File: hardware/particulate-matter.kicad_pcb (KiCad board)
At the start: 2 copper layers, 70 x 40 mm, 36 parts, among them P1 CON-SENSOR2, P2 BOOT, P3 DEBUG, U1 XMC1XXX48, U2 DRILL, U3 DRILL, U4 DRILL, U5 DRILL, U6 PMS7003, X1 16MHz

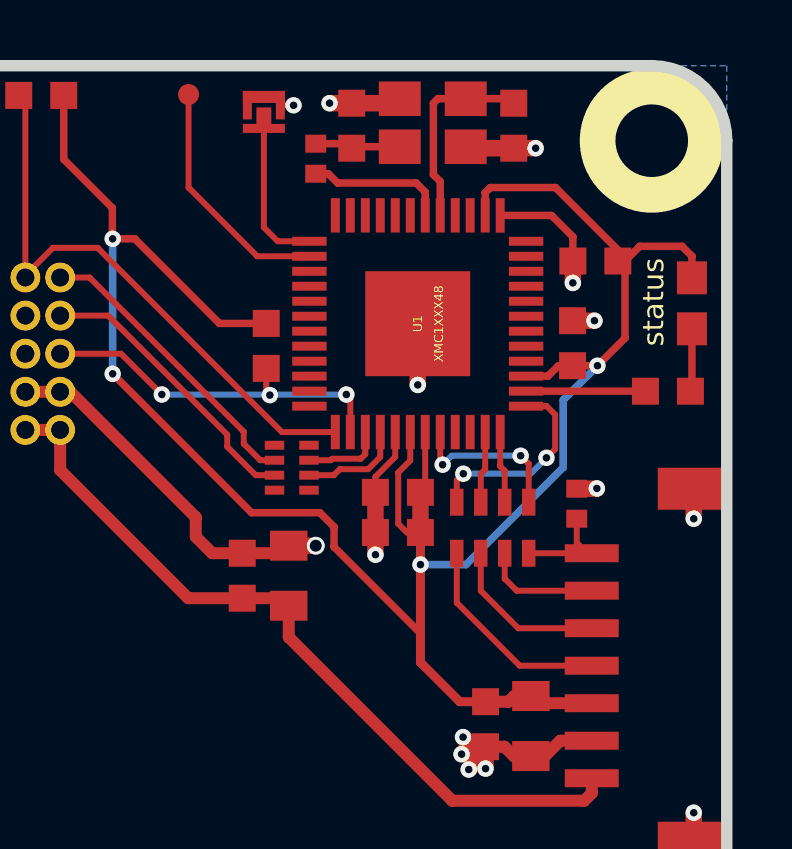
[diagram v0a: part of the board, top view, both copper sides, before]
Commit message: Remove R2, change footprint of RP1
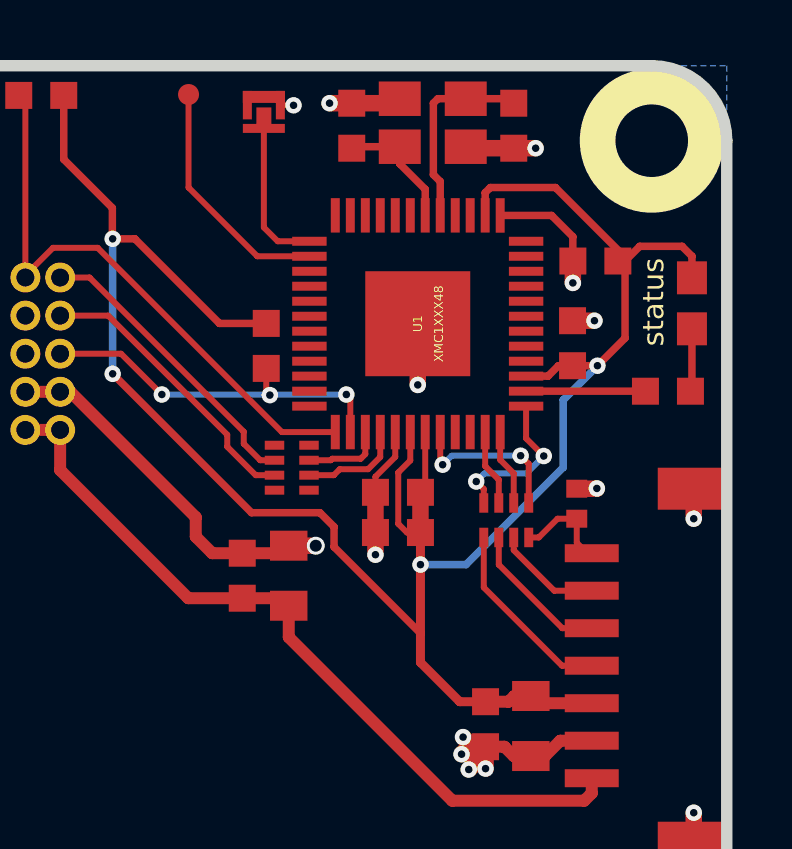
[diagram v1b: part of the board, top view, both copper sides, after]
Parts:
- removed R9: 0, kicad-libraries:R0402F
- RP1: footprint kicad-libraries:0603X4 -> kicad-libraries:4X0402
- moved RP1 0.51 mm to (163.4, 80.2), turned to 0 degrees
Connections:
- U1 pad 42: Net-(R9-Pad1) -> Net-(C9-Pad1)
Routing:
- net Net-(R9-Pad1): track 4.68 -> 0.00 mm
- net Net-(C9-Pad1): track 2.88 -> 4.47 mm
- net S-CS: track 6.67 -> 5.33 mm
- net Net-(P1-Pad4): track 7.02 -> 6.35 mm
- net Net-(P1-Pad5): track 5.47 -> 4.88 mm

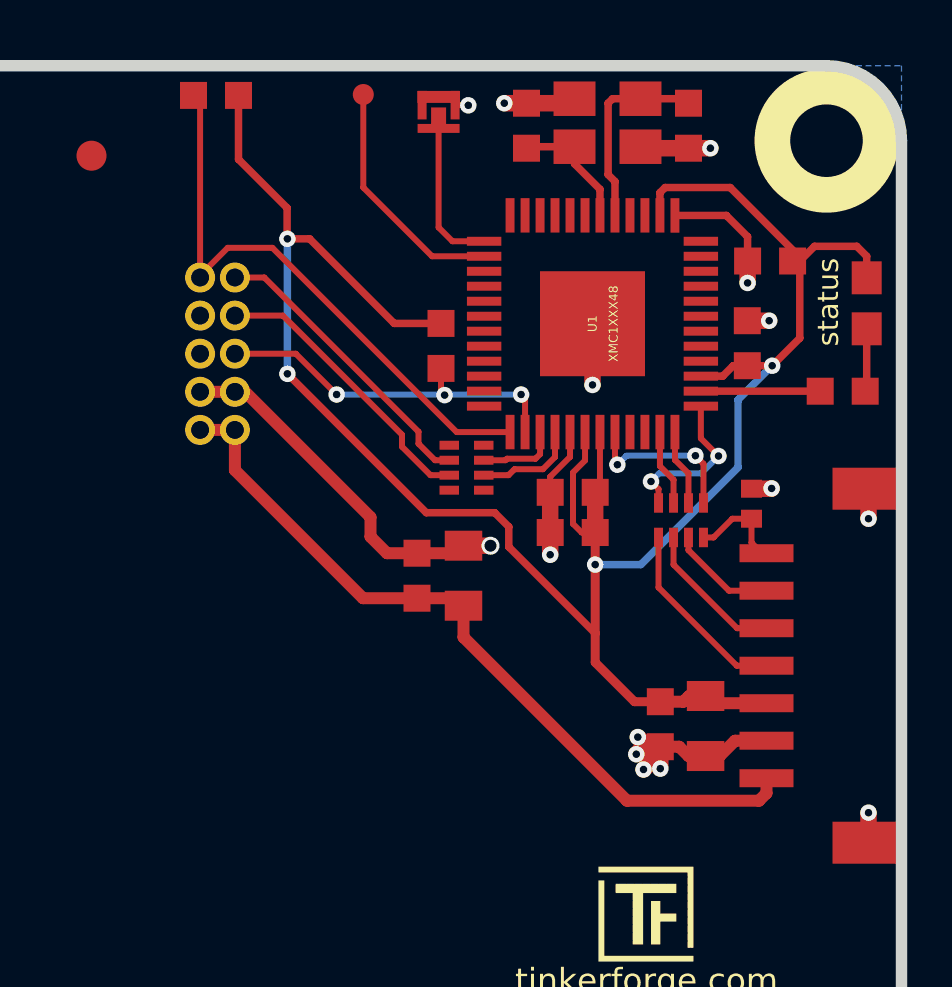
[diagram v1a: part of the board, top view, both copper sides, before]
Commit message: Fix ground routing of U6, move debug pad & C10-C11, move U6 to the edge
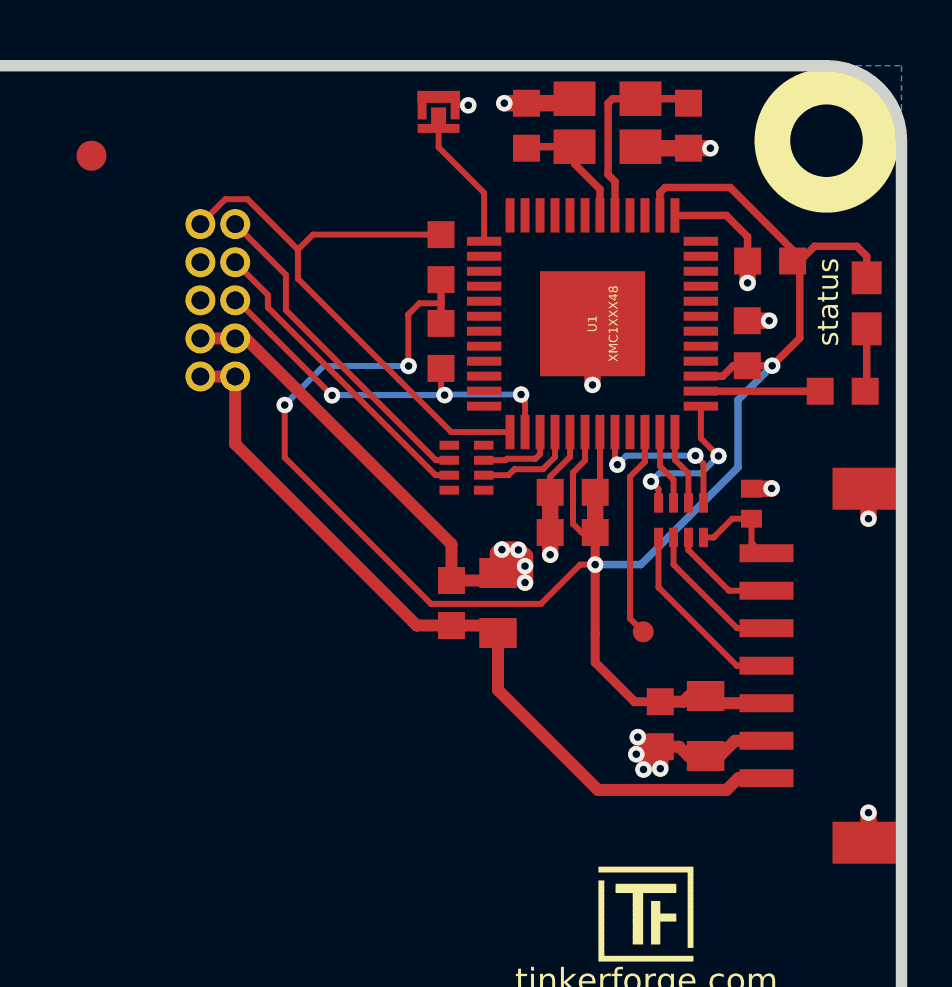
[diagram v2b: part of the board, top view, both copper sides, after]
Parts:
- moved P3 20.2 mm to (162.2, 83.9)
- moved R2 9.24 mm to (155.4, 71.4), turned to 90 degrees
- moved U6 1.78 mm to (130.3, 83.3)
- moved C10 1.47 mm to (155.8, 82.9)
- moved C11 1.47 mm to (157.3, 82.9)
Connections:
- U1 pad 2: Net-(P3-Pad1) -> Net-(U1-Pad2)
- U1 pad 22: Net-(U1-Pad22) -> Net-(P3-Pad1)
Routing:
- net VCC: track 74.9 -> 68.2 mm
- net GND: track 40.9 -> 47.5 mm, vias 15 -> 18
- net Net-(RP2-Pad2): track 9.90 -> 11.1 mm
- net +5V: track 26.2 -> 27.2 mm
- net Net-(P3-Pad1): track 8.08 -> 7.05 mm
- net Net-(P2-Pad2): track 5.81 -> 4.79 mm
- net PMS_RESET: track 12.4 -> 13.2 mm
- net Net-(RP2-Pad3): track 9.58 -> 10.3 mm
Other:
- rule trace_min: 0.2 -> 0

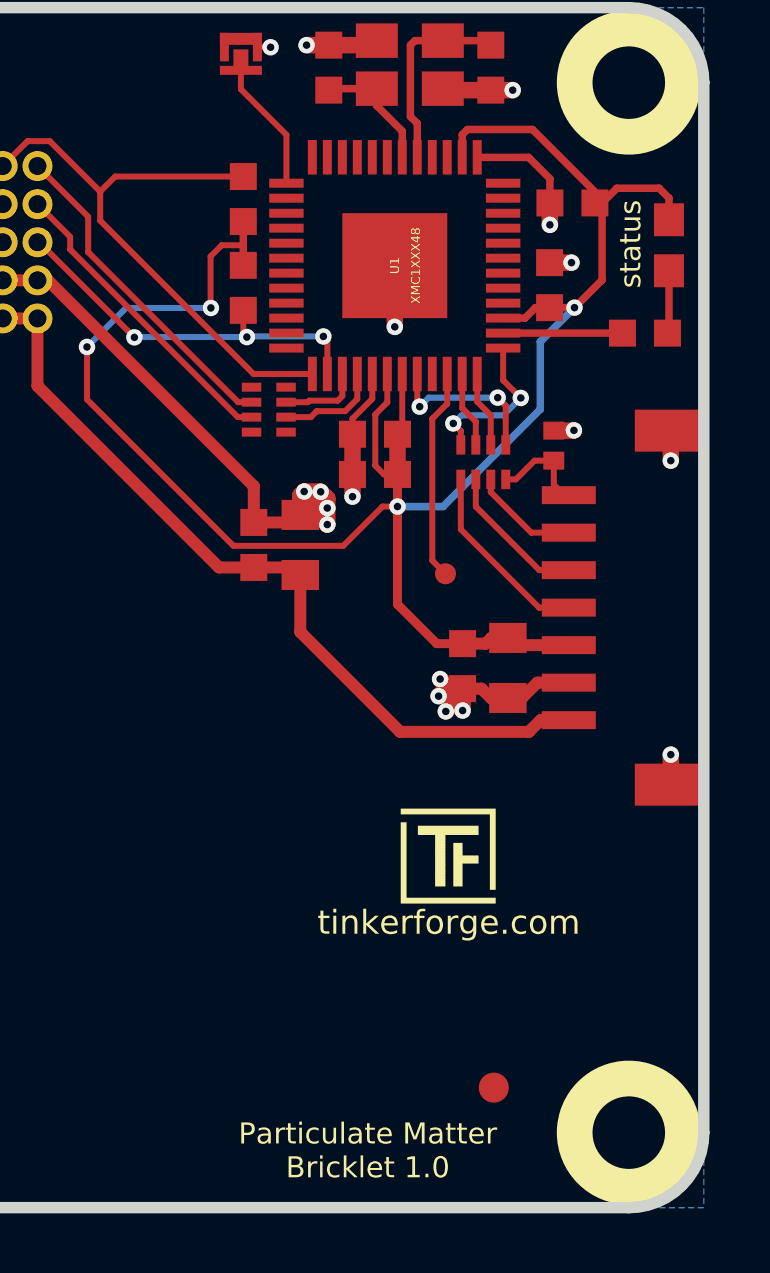
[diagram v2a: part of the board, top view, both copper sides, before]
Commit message: fix Status text, fix board name
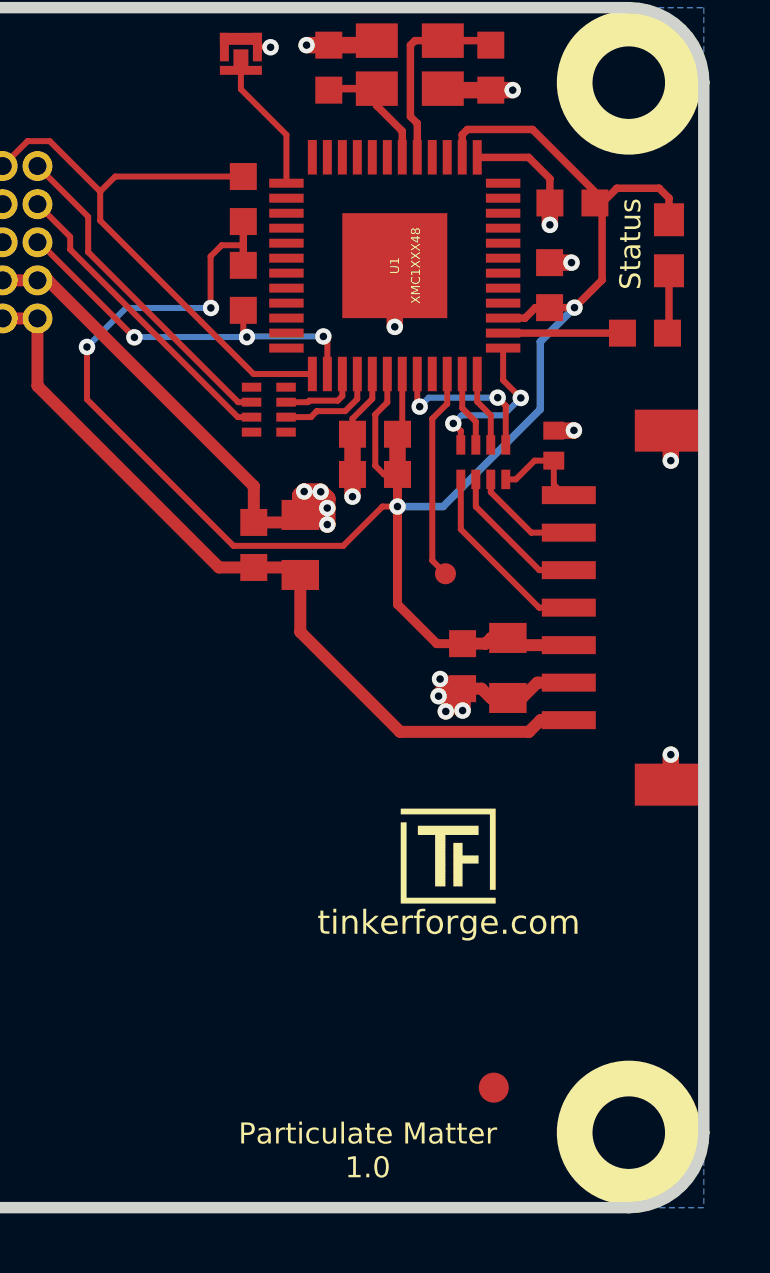
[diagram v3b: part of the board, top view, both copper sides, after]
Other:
- board text added: "Particulate Matter 1.0"
- board text added: "Status"
- board text removed: "Particulate Matter Bricklet 1.0"
- board text removed: "status"
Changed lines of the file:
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@@
-(kicad_pcb (version 4) (host pcbnew 4.0.2+dfsg1-stable)
+(kicad_pcb (version 4) (host pcbnew 4.0.7-e2-6376~58~ubuntu17.04.1)
   (general
     (links 66)
@@
   )
   (setup
-    (last_trace_width 0.2)
+    (last_trace_width 0.25)
     (user_trace_width 0.2)
     (user_trace_width 0.25)
@@
     (visible_elements FFFFFF7F)
     (pcbplotparams
-      (layerselection 0x00030_80000001)
+      (layerselection 0x010f8_80000001)
       (usegerberextensions false)
       (excludeedgelayer true)
@@
       (psnegative false)
       (psa4output false)
-      (plotreference true)
-      (plotvalue true)
+      (plotreference false)
+      (plotvalue false)
       (plotinvisibletext false)
       (padsonsilk false)
@@
       (outputformat 1)
       (mirror false)
-      (drillshape 1)
+      (drillshape 0)
       (scaleselection 1)
-      (outputdirectory ""))
+      (outputdirectory /tmp/bla))
   )
   (net 0 "")
@@
     )
   )
-  (gr_text "Particulate Matter\nBricklet 1.0" (at 159.6 103.1) (layer F.SilkS)
+  (gr_text "Particulate Matter\n1.0" (at 159.6 103.1) (layer F.SilkS)
     (effects (font (size 0.7 0.7) (thickness 0.15)))
   )
@@
     (effects (font (size 0.8 0.8) (thickness 0.15)))
   )
-  (gr_text status (at 168.36 72.88 90) (layer F.SilkS)
+  (gr_text Status (at 168.36 72.88 90) (layer F.SilkS)
     (effects (font (size 0.7 0.7) (thickness 0.15)))
   )
@@
     (polygon
       (pts
-        (xy 149.29 76.06) (xy 146.73 76.06) (xy 146.73 69.58) (xy 149.29 69.58) (xy 149.29 76.06)
+        (xy 149.29 76.06) (xy 146.73 76.06) (xy 146.73 69.58) (xy 149.29 69.58)
       )
     )

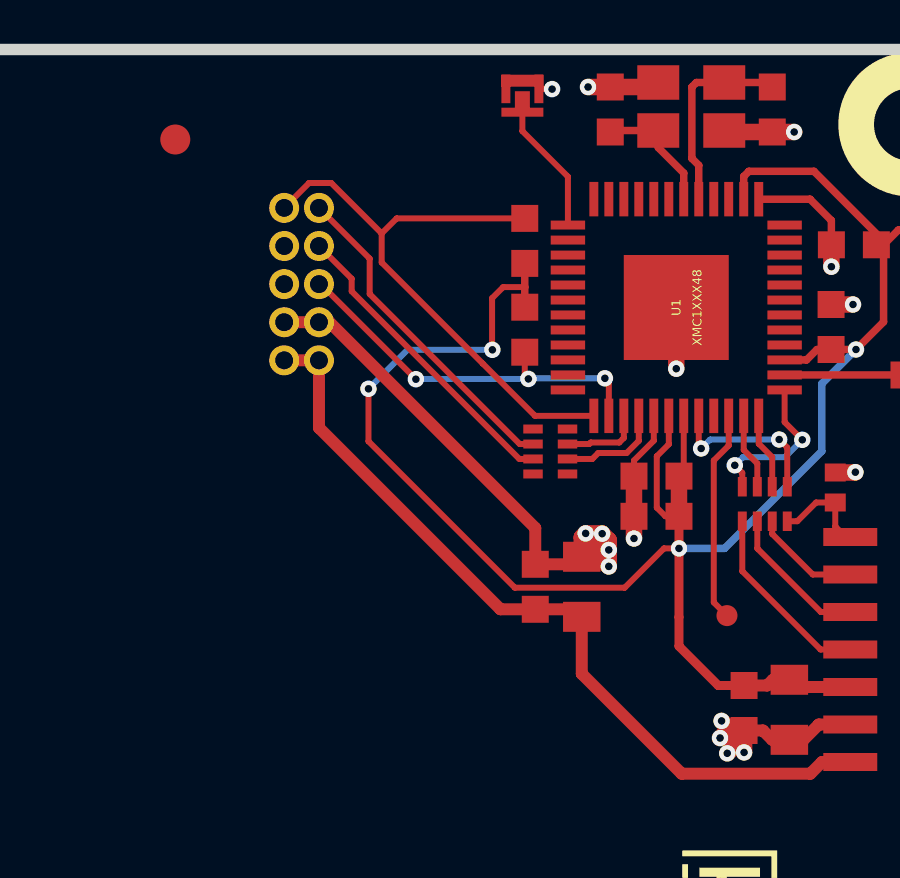
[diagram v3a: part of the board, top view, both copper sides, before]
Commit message: implement fixed footprint
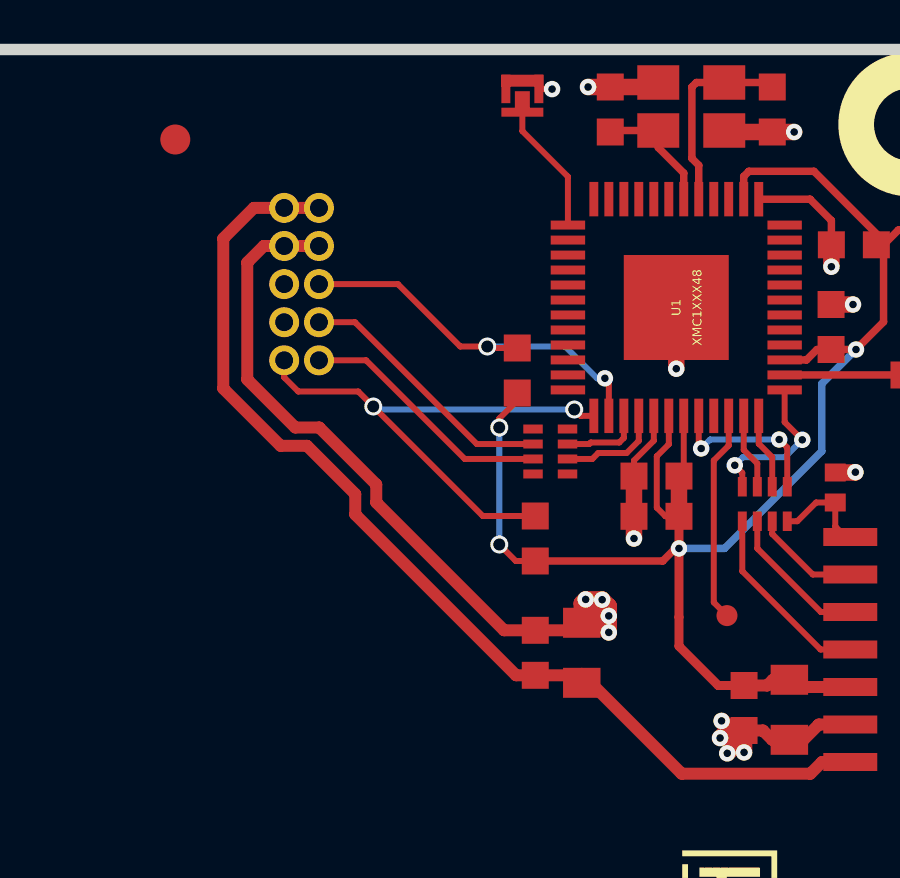
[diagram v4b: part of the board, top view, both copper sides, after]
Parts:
- moved R2 9.93 mm to (155.8, 81.3)
- moved C10 2.20 mm to (155.8, 85.1)
- moved C11 2.20 mm to (157.3, 85.1)
- moved R3 1.38 mm to (155.2, 75.7), turned to 90 degrees
- turned RP2 to 90 degrees
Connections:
- RP2 pad 2: Net-(RP2-Pad2) -> PMS_RX
- RP2 pad 3: Net-(RP2-Pad3) -> PMS_TX
- RP2 pad 6: PMS_RX -> Net-(RP2-Pad6)
- RP2 pad 7: PMS_TX -> Net-(RP2-Pad7)
- U6 pad 7: Net-(RP2-Pad3) -> Net-(RP2-Pad6)
- U6 pad 9: Net-(RP2-Pad2) -> Net-(RP2-Pad7)
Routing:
- net VCC: track 68.2 -> 56.1 mm
- net Net-(RP2-Pad2): track 11.1 -> 0.00 mm
- net Net-(RP2-Pad3): track 10.3 -> 0.00 mm
- net Net-(RP2-Pad6): track 0.00 -> 8.82 mm
- net Net-(RP2-Pad7): track 0.00 -> 8.50 mm
- net +5V: track 27.2 -> 35.6 mm
- net GND: track 47.5 -> 55.0 mm
- net PMS_SET: track 19.4 -> 18.3 mm, vias 0 -> 2
- net PMS_RESET: vias 3 -> 2

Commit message: fix logo positions
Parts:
- moved VAL 10.2 mm to (135.8, 85.0)
- moved VAL 10.0 mm to (125.8, 85.0)
- moved G*** 0.20 mm to (145.8, 85.0)
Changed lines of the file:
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@@
     (links 66)
     (no_connects 0)
-    (area 100.609499 64.809499 170.990501 105.190501)
+    (area 14.621426 64.145139 171.654861 193.825)
     (thickness 1.6)
     (drawings 12)
@@
   )
   (setup
-    (last_trace_width 0.4)
+    (last_trace_width 0.25)
     (user_trace_width 0.2)
     (user_trace_width 0.25)
@@
   )
   (module kicad-libraries:Logo_CoMCU (layer B.Cu)
-    (at 146 85 180)
+    (at 145.8 85 180)
     (fp_text reference G*** (at 0 0 180) (layer B.SilkS) hide
       (effects (font (thickness 0.3)) (justify mirror))
@@
   )
   (module kicad-libraries:CE_5mm (layer B.Cu)
-    (at 135.8 85 180)
+    (at 125.8 85 180)
     (fp_text reference VAL (at 0 0 180) (layer B.SilkS) hide
       (effects (font (size 0.2 0.2) (thickness 0.05)) (justify mirror))
@@
   )
   (module kicad-libraries:WEEE_7mm (layer B.Cu)
-    (at 125.6 85 180)
+    (at 135.8 85 180)
     (fp_text reference VAL (at 0 0 180) (layer B.SilkS) hide
       (effects (font (size 0.2 0.2) (thickness 0.05)) (justify mirror))

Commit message: specify processor
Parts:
- U1: value XMC1XXX48 -> XMC1404
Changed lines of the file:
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@@
   (module kicad-libraries:QFN48-EP2 (layer F.Cu)
     (at 160.5 73.6 270)
-    (fp_text reference U1 (at 0 0 270) (layer F.SilkS)
-      (effects (font (size 0.29972 0.29972) (thickness 0.0762)))
+    (fp_text reference U1 (at 0 0 270) (layer F.Fab)
+      (effects (font (size 0.29972 0.29972) (thickness 0.07493)))
     )
-    (fp_text value XMC1XXX48 (at 0 -0.7 270) (layer F.SilkS)
-      (effects (font (size 0.29972 0.29972) (thickness 0.0762)))
+    (fp_text value XMC1404 (at 0 -0.7 270) (layer F.Fab)
+      (effects (font (size 0.29972 0.29972) (thickness 0.07493)))
     )
     (fp_circle (center -2.5 2.6) (end -2.4 2.8) (layer F.Fab) (width 0.05))
